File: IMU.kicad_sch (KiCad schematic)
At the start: 4 parts

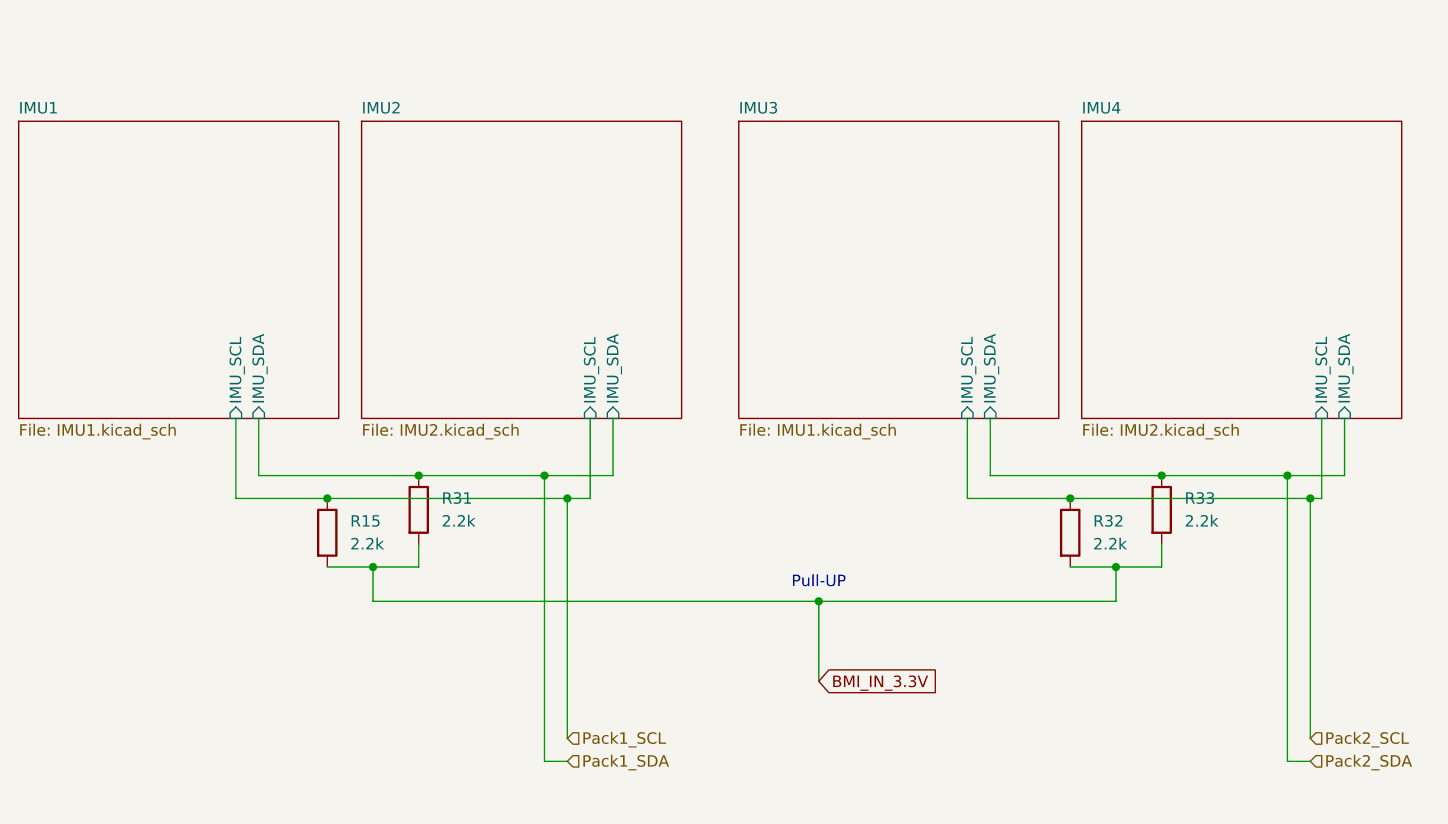
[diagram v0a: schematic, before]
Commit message: new outline of board plus first traces
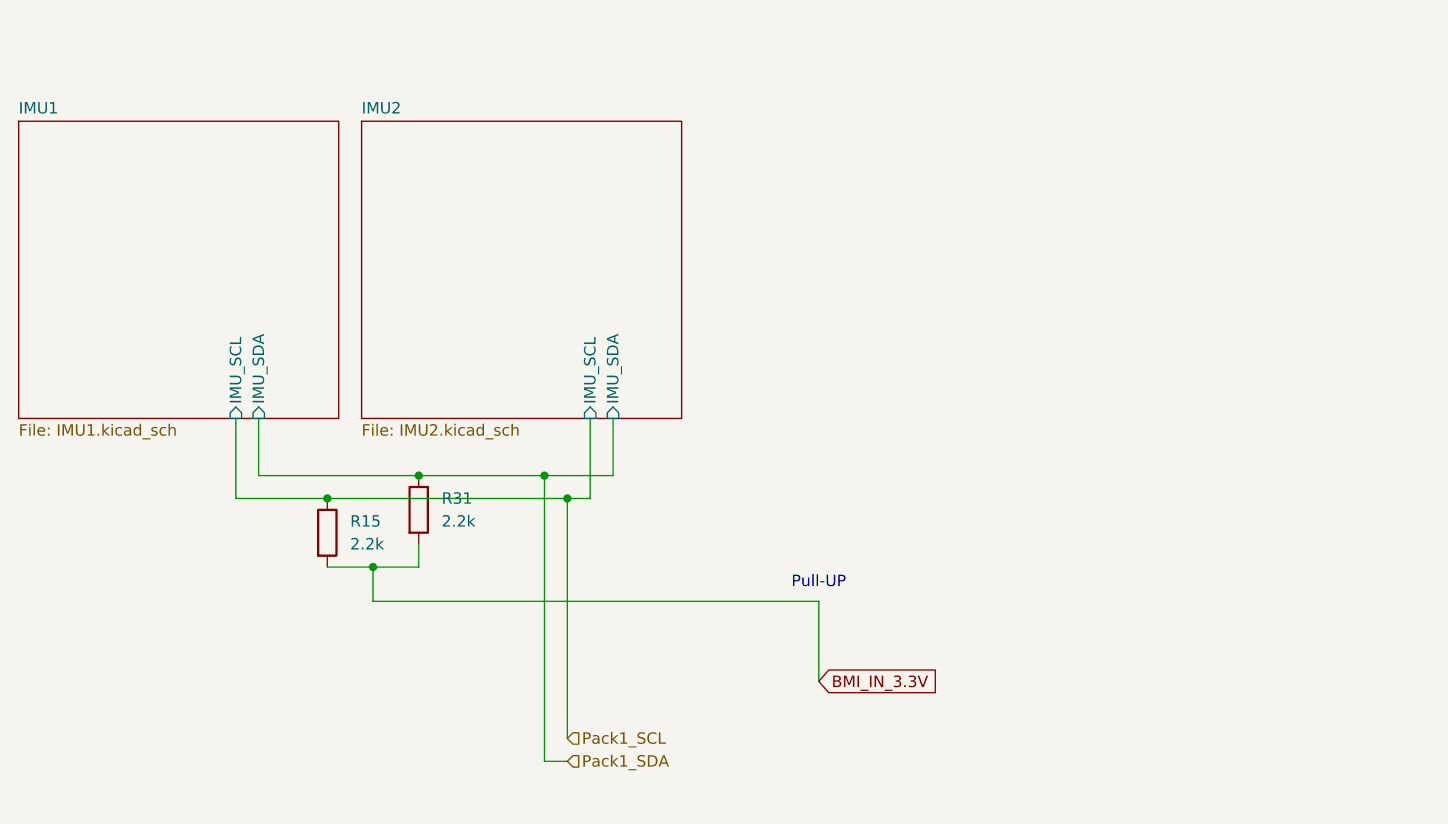
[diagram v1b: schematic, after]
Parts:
- removed R32, R33: 2.2k, Resistor_SMD:R_0603_1608Metric, symbol #dzdb:g_res/R-2.2k-0603
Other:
- removed sheet IMU3
- removed sheet IMU4

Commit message: chore: Many routing changes
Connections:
- net BMI_IN_3.3V renamed +3.3V
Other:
- sheet IMU1 ports: added BMI_In_3.3V; removed none
- sheet IMU2 ports: added BMI_In_3.3V; removed none
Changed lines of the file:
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@@
 	(text "Pull-UP"
 		(exclude_from_sim no)
-		(at 152.4 104.648 0)
+		(at 91.44 104.394 0)
 		(effects
 			(font
@@
 			)
 		)
+	)
+	(junction
+		(at 127 95.25)
+		(diameter 0)
+		(color 0 0 0 0)
 	)
 	(junction
@@
 	)
 	(junction
+		(at 142.24 66.04)
+		(diameter 0)
+		(color 0 0 0 0)
+	)
+	(junction
 		(at 97.79 95.25)
 		(diameter 0)
@@
 	)
 	(junction
-		(at 124.46 95.25)
+		(at 129.54 92.71)
+		(diameter 0)
+		(color 0 0 0 0)
+	)
+	(junction
+		(at 142.24 106.68)
 		(diameter 0)
 		(color 0 0 0 0)
@@
 		(color 0 0 0 0)
 	)
-	(junction
-		(at 121.92 92.71)
-		(diameter 0)
-		(color 0 0 0 0)
-	)
-	(wire
-		(pts
-			(xy 124.46 124.46) (xy 121.92 124.46)
-		)
-		(stroke
-			(width 0)
-			(type default)
-		)
-	)
-	(wire
-		(pts
-			(xy 124.46 95.25) (xy 124.46 121.92)
+	(wire
+		(pts
+			(xy 142.24 66.04) (xy 142.24 106.68)
+		)
+		(stroke
+			(width 0)
+			(type default)
+		)
+	)
+	(wire
+		(pts
+			(xy 96.52 48.26) (xy 142.24 48.26)
+		)
+		(stroke
+			(width 0)
+			(type default)
+		)
+	)
+	(wire
+		(pts
+			(xy 127 95.25) (xy 127 101.6)
 		)
 		(stroke
@@
 	(wire
 		(pts
-			(xy 127 95.25) (xy 124.46 95.25)
-		)
-		(stroke
-			(width 0)
-			(type default)
-		)
-	)
-	(wire
-		(pts
-			(xy 152.4 115.57) (xy 152.4 106.68)
-		)
-		(stroke
-			(width 0)
-			(type default)
-		)
-	)
-	(wire
-		(pts
 			(xy 97.79 95.25) (xy 87.63 95.25)
 		)
@@
 	(wire
 		(pts
-			(xy 124.46 95.25) (xy 97.79 95.25)
+			(xy 97.79 95.25) (xy 127 95.25)
 		)
 		(stroke
@@
 	(wire
 		(pts
-			(xy 107.95 92.71) (xy 121.92 92.71)
+			(xy 107.95 92.71) (xy 129.54 92.71)
+		)
+		(stroke
+			(width 0)
+			(type default)
+		)
+	)
+	(wire
+		(pts
+			(xy 142.24 66.04) (xy 137.16 66.04)
+		)
+		(stroke
+			(width 0)
+			(type default)
+		)
+	)
+	(wire
+		(pts
+			(xy 142.24 106.68) (xy 102.87 106.68)
 		)
 		(stroke
@@
 	(wire
 		(pts
+			(xy 96.52 53.34) (xy 96.52 48.26)
+		)
+		(stroke
+			(width 0)
+			(type default)
+		)
+	)
+	(wire
+		(pts
 			(xy 107.95 100.33) (xy 107.95 102.87)
 		)
@@
 	(wire
 		(pts
-			(xy 121.92 92.71) (xy 121.92 124.46)
+			(xy 129.54 92.71) (xy 129.54 99.06)
+		)
+		(stroke
+			(width 0)
+			(type default)
+		)
+	)
+	(wire
+		(pts
+			(xy 142.24 48.26) (xy 142.24 66.04)
 		)
 		(stroke
@@
 	(wire
 		(pts
-			(xy 152.4 106.68) (xy 102.87 106.68)
-		)
-		(stroke
-			(width 0)
-			(type default)
-		)
-	)
-	(wire
-		(pts
-			(xy 121.92 92.71) (xy 129.54 92.71)
-		)
-		(stroke
-			(width 0)
-			(type default)
-		)
-	)
-	(global_label "BMI_IN_3.3V"
+			(xy 152.4 106.68) (xy 142.24 106.68)
+		)
+		(stroke
+			(width 0)
+			(type default)
+		)
+	)
+	(hierarchical_label "Pack1_SDA"
 		(shape input)
-		(at 152.4 115.57 0)
-		(fields_autoplaced yes)
+		(at 129.54 99.06 0)
 		(effects
 			(font
@@
 			(justify left)
 		)
-		(property "Intersheetrefs" "${INTERSHEET_REFS}"
-			(at 166.6943 115.57 0)
-			(effects
-				(font
-					(size 1.27 1.27)
-				)
-				(justify left)
-				(hide yes)
-			)
-		)
-	)
-	(hierarchical_label "Pack1_SDA"
-		(shape input)
-		(at 124.46 124.46 0)
-		(effects
-			(font
-				(size 1.27 1.27)
-			)
-			(justify left)
-		)
 	)
 	(hierarchical_label "Pack1_SCL"
 		(shape input)
-		(at 124.46 121.92 0)
+		(at 127 101.6 0)
 		(effects
 			(font
@@
 	)
 	(symbol
+		(lib_id "power:+3.3V")
+		(at 152.4 106.68 0)
+		(unit 1)
+		(exclude_from_sim no)
+		(in_bom yes)
+		(on_board yes)
+		(dnp no)
+		(fields_autoplaced yes)
+		(property "Reference" "#PWR033"
+			(at 152.4 110.49 0)
+			(effects
+				(font
+					(size 1.27 1.27)
+				)
+				(hide yes)
+			)
+		)
+		(property "Value" "+3.3V"
+			(at 152.4 101.6 0)
+			(effects
+				(font
+					(size 1.27 1.27)
+				)
+			)
+		)
+		(property "Footprint" ""
+			(at 152.4 106.68 0)
+			(effects
+				(font
+					(size 1.27 1.27)
+				)
+				(hide yes)
+			)
+		)
+		(property "Datasheet" ""
+			(at 152.4 106.68 0)
+			(effects
+				(font
+					(size 1.27 1.27)
+				)
+				(hide yes)
+			)
+		)
+		(property "Description" "Power symbol creates a global label with name \"+3.3V\""
+			(at 152.4 106.68 0)
+			(effects
+				(font
+					(size 1.27 1.27)
+				)
+				(hide yes)
+			)
+		)
+		(pin "1"
+		)
+		(instances
+			(project ""
+				(path "/ce1819b2-f280-40ed-834f-6fe4d12f809d/bdf8f7d6-a5ee-4741-925d-5019e8cbdfce"
+					(reference "#PWR033")
+					(unit 1)
+				)
+			)
+		)
+	)
+	(symbol
 		(lib_id "#dzdb:g_res/R-2.2k-0603")
 		(at 107.95 96.52 0)
@@
 			)
 		)
+		(pin "BMI_In_3.3V" input
+			(at 96.52 53.34 90)
+			(effects
+				(font
+					(size 1.27 1.27)
+				)
+				(justify right)
+			)
+		)
 		(instances
 			(project "nautilus_mainboard"
@@
 			)
 		)
+		(pin "BMI_In_3.3V" input
+			(at 137.16 66.04 0)
+			(effects
+				(font
+					(size 1.27 1.27)
+				)
+				(justify right)
+			)
+		)

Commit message: chore: more cleanup
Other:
- company: (none) -> Davide
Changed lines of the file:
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@@
 	(generator_version "9.0")
 	(paper "A4")
+	(title_block
+		(date "2025-11-18")
+		(company "Davide")
+	)
 	(text "Pull-UP"
 		(exclude_from_sim no)

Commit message: chore: Loads of redoing stuff. Added a Changelog
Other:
- title: (none) -> Nautilus_Mainboard
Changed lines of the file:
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@@
 	(paper "A4")
 	(title_block
+		(title "Nautilus_Mainboard")
 		(date "2025-11-19")
 		(rev "0")

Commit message: chore: finalized routing
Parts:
- removed R15, R31: 2.2k, Resistor_SMD:R_0603_1608Metric, symbol #dzdb:g_res/R-2.2k-0603
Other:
- sheet IMU1 ports: added BLI_SCK, BMI_CSB_ACCEL, BMI_CSB_GYRO, BMI_MISO, BMI_MOSI; removed IMU_SCL, IMU_SDA
- sheet IMU2: file IMU2.kicad_sch -> IMU1.kicad_sch
- sheet IMU2 ports: added BLI_SCK, BMI_CSB_ACCEL, BMI_CSB_GYRO, BMI_MISO, BMI_MOSI; removed IMU_SCL, IMU_SDA
- note removed: "Pull-UP"
